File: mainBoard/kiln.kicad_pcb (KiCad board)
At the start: 4 copper layers, 203.1 x 114.5 mm, 214 parts, among them IC4 MAXM17572AMC+T, IC5 MAXM17572AMC+T, IC6 MAXM17572AMC+T, IC7 MAXM17572AMC+T, J1 1935161, J10 1935174, J11 1935174, J12 1935161, J13 SJ2-35813B-SMT-TR, J14 1935161, J15 SJ2-35813B-SMT-TR, J16 1935161, J17 SJ2-35813B-SMT-TR, J18 1935161, J19 1935161, J2 Conn_01x10_Pin, J20 1935161, J21 1935161, J23 1935161, J24 1935161, J25 1935161, J3 1935174, J4 1935174, J6 Conn_01x20_Socket, J7 Conn_02x06_Odd_Even, J8 1935174, K1 EE2-12NUH, K2 EE2-12NUH, K3 EE2-12NUH, K4 EE2-12NUH, K5 EE2-12NUH, Q1 BSS138P,215, Q2 BSS138P,215, Q3 BSS138P,215, Q4 BSS138P,215, Q5 BSS138P,215, U1 TCMT1109, U13 TCMT1109, U14 TCMT1109, U2 TCMT1109, U3 TCMT1109, U4 ESP32-S3-DevKitC, U5 SX1509, U7 AD8542, U8 AD8542, U9 AD8542

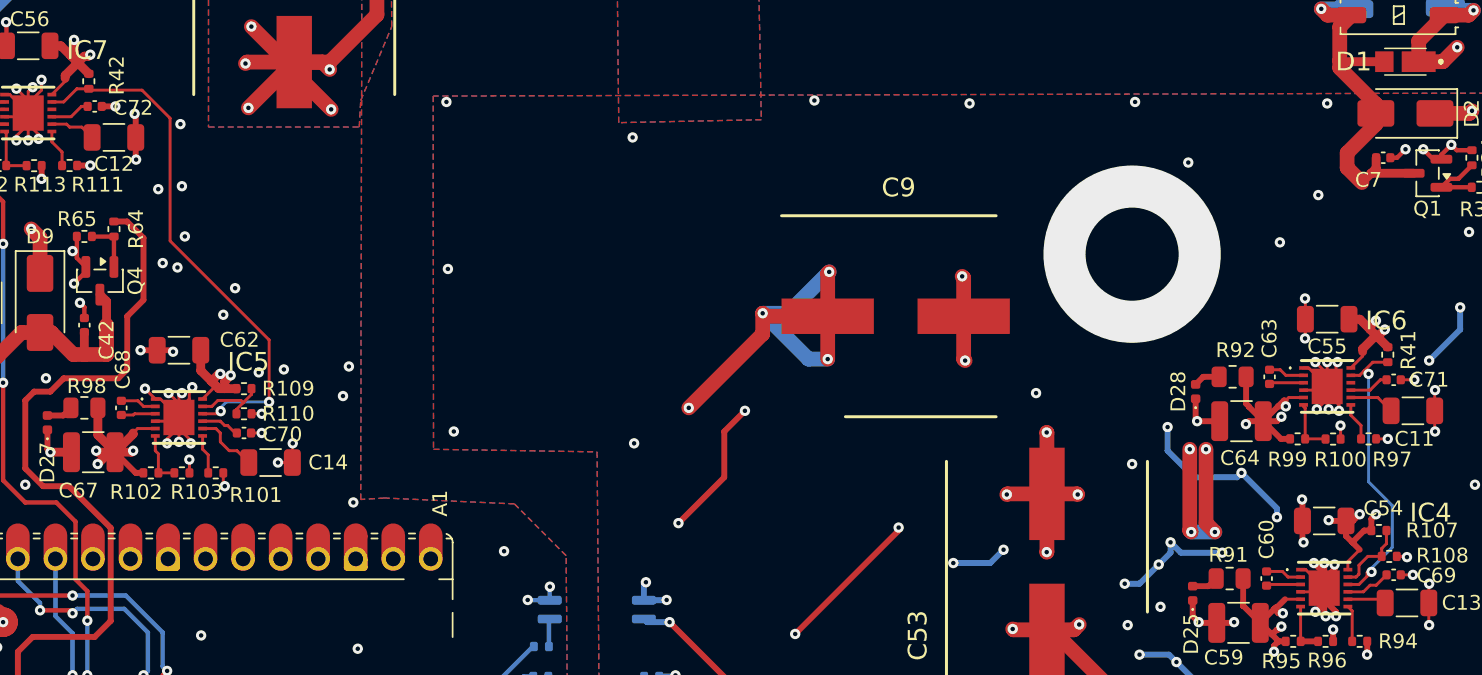
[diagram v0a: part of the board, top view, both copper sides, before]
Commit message: Update Board. removed power sequencing of 5v because it violated the voltage range of the power supply reset pin
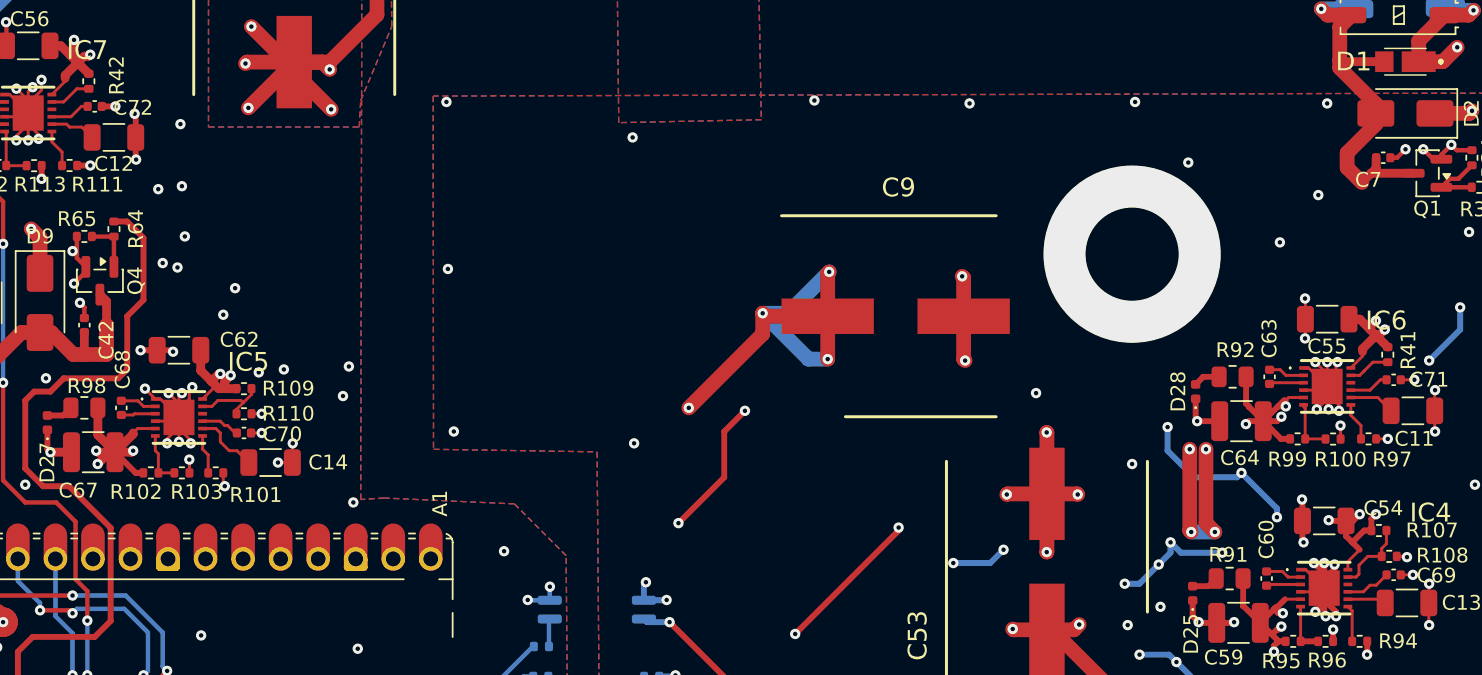
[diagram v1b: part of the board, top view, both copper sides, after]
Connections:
- IC4 pad 10: /5V Regulator/EN -> /MainRegulator/RESET
- IC5 pad 10: /Safty 5V Regulator/EN -> /SaftyRegulator/RESET
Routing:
- net /Safty 5V Regulator/EN: track 36.2 -> 3.00 mm, vias 2 -> 0
- net /5V Regulator/EN: track 20.0 -> 2.87 mm, vias 2 -> 0
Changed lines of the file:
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@@
 			(size 0.25 0.6)
 			(layers "F.Cu" "F.Mask" "F.Paste")
-			(net "/5V Regulator/EN")
+			(net "/MainRegulator/RESET")
 			(pinfunction "~{RESET}_10")
 			(pintype "passive")
@@
 			(size 0.25 0.6)
 			(layers "F.Cu" "F.Mask" "F.Paste")
-			(net "/Safty 5V Regulator/EN")
+			(net "/SaftyRegulator/RESET")
 			(pinfunction "~{RESET}_10")
 			(pintype "passive")
@@
 	)
 	(segment
-		(start 174.05 99.45)
-		(end 173.3 99.45)
-		(width 0.2)
-		(layer "F.Cu")
-		(net "/5V Regulator/EN")
-	)
-	(segment
 		(start 174.4 85)
 		(end 174.99 84.41)
@@
 	)
 	(segment
-		(start 174.6 98.65)
-		(end 174.6 98.9)
-		(width 0.2)
-		(layer "F.Cu")
-		(net "/5V Regulator/EN")
-	)
-	(segment
 		(start 174.99 84.41)
 		(end 176 84.41)
@@
 	)
 	(segment
-		(start 174.6 98.9)
-		(end 174.05 99.45)
-		(width 0.2)
-		(layer "F.Cu")
-		(net "/5V Regulator/EN")
-	)
-	(segment
-		(start 174.5 85)
-		(end 174.7 85.2)
-		(width 0.2)
-		(layer "F.Cu")
-		(net "/5V Regulator/EN")
-	)
-	(segment
 		(start 174.1 85.3)
 		(end 174.4 85)
@@
 	)
 	(segment
-		(start 174.65 98.6)
-		(end 174.6 98.65)
-		(width 0.2)
-		(layer "F.Cu")
-		(net "/5V Regulator/EN")
-	)
-	(segment
-		(start 174.4 85)
-		(end 174.5 85)
-		(width 0.2)
-		(layer "F.Cu")
-		(net "/5V Regulator/EN")
-	)
-	(segment
-		(start 174.9 98.6)
-		(end 174.65 98.6)
-		(width 0.2)
-		(layer "F.Cu")
-		(net "/5V Regulator/EN")
-	)
-	(segment
 		(start 173.5 85.3)
 		(end 174.1 85.3)
@@
 		(net "/5V Regulator/EN")
 	)
-	(via
-		(at 174.7 85.2)
-		(size 0.7)
-		(drill 0.3)
-		(layers "F.Cu" "B.Cu")
-		(net "/5V Regulator/EN")
-	)
-	(via
-		(at 174.9 98.6)
-		(size 0.7)
-		(drill 0.3)
-		(layers "F.Cu" "B.Cu")
-		(net "/5V Regulator/EN")
-	)
-	(segment
-		(start 174.7 92.5)
-		(end 174.7 85.2)
-		(width 0.2)
-		(layer "B.Cu")
-		(net "/5V Regulator/EN")
-	)
-	(segment
-		(start 174.9 98.6)
-		(end 174.9 98.35)
-		(width 0.2)
-		(layer "B.Cu")
-		(net "/5V Regulator/EN")
-	)
-	(segment
-		(start 174.9 98.35)
-		(end 176.3 96.95)
-		(width 0.2)
-		(layer "B.Cu")
-		(net "/5V Regulator/EN")
-	)
-	(segment
-		(start 176.3 94.1)
-		(end 174.7 92.5)
-		(width 0.2)
-		(layer "B.Cu")
-		(net "/5V Regulator/EN")
-	)
-	(segment
-		(start 176.3 96.95)
-		(end 176.3 94.1)
-		(width 0.2)
-		(layer "B.Cu")
-		(net "/5V Regulator/EN")
-	)
 	(segment
 		(start 173.6 96.6)
@@
 	)
 	(segment
-		(start 100.3 82.9)
-		(end 100.3 87.1)
-		(width 0.2)
-		(layer "F.Cu")
-		(net "/Safty 5V Regulator/EN")
-	)
-	(segment
-		(start 93.6 76.2)
-		(end 100.3 82.9)
-		(width 0.2)
-		(layer "F.Cu")
-		(net "/Safty 5V Regulator/EN")
-	)
-	(segment
 		(start 87.29 65.91)
 		(end 88.1 65.91)
@@
 	)
 	(segment
-		(start 95.8 87.9)
-		(end 96.84853 87.9)
-		(width 0.2)
-		(layer "F.Cu")
-		(net "/Safty 5V Regulator/EN")
-	)
-	(segment
 		(start 85.6 66.8)
 		(end 86.4 66.8)
@@
 	)
 	(segment
-		(start 91.7 66)
-		(end 93.6 67.9)
-		(width 0.2)
-		(layer "F.Cu")
-		(net "/Safty 5V Regulator/EN")
-	)
-	(segment
-		(start 96.84853 87.9)
-		(end 97.024265 87.724265)
-		(width 0.2)
-		(layer "F.Cu")
-		(net "/Safty 5V Regulator/EN")
-	)
-	(segment
-		(start 88.19 66)
-		(end 91.7 66)
-		(width 0.2)
-		(layer "F.Cu")
-		(net "/Safty 5V Regulator/EN")
-	)
-	(segment
 		(start 86.4 66.8)
 		(end 87.29 65.91)
@@
 	)
 	(segment
-		(start 93.6 67.9)
-		(end 93.6 76.2)
-		(width 0.2)
-		(layer "F.Cu")
-		(net "/Safty 5V Regulator/EN")
-	)
-	(via
-		(at 100.3 87.1)
-		(size 0.7)
-		(drill 0.3)
-		(layers "F.Cu" "B.Cu")
-		(net "/Safty 5V Regulator/EN")
-	)
-	(via
-		(at 97.024265 87.724265)
-		(size 0.7)
-		(drill 0.3)
-		(layers "F.Cu" "B.Cu")
-		(net "/Safty 5V Regulator/EN")
-	)
-	(segment
-		(start 97.4 87.1)
-		(end 96.9 87.6)
-		(width 0.2)
-		(layer "B.Cu")
-		(net "/Safty 5V Regulator/EN")
-	)
-	(segment
-		(start 96.9 87.6)
-		(end 97.024265 87.724265)
-		(width 0.2)
-		(layer "B.Cu")
-		(net "/Safty 5V Regulator/EN")
-	)
-	(segment
-		(start 100.3 87.1)
-		(end 97.4 87.1)
-		(width 0.2)
-		(layer "B.Cu")
-		(net "/Safty 5V Regulator/EN")
-	)
-	(segment
 		(start 192 71.75)
 		(end 192.25 72)
@@
 	)
 	(group ""
-		(members "0f56723d-3be1-4363-aa22-d1860701c7dc" "6eccc95b-070c-44a6-b1f1-dab8a373bad4"
-			"ecd03097-544e-4ff1-9250-bd5f418e28c1"
+		(members "0f56723d-3be1-4363-aa22-d1860701c7dc" "5a2fada0-188b-484a-bad7-1807c7aed6e5"
+			"6eccc95b-070c-44a6-b1f1-dab8a373bad4" "ecd03097-544e-4ff1-9250-bd5f418e28c1"
 		)
 	)
@@
 	)
 	(group ""
+		(members "396ff842-1671-4172-bf05-e17732549ce8" "4fc6aa10-2ebe-4c37-b5bb-b0deef5bf880"
+			"937600a3-2b20-4705-b469-8f8dcff22017" "b32b362c-9a1f-4c29-b6b9-67d3c509b282"
+		)
+	)
+	(group ""
 		(members "1354254c-1560-4867-a241-d6e0818e9545" "1dd019e7-ef0a-4e37-a044-a9138c332660"
 			"2d0f587a-aa5a-4280-accb-adcb2943fcc1" "61dba97c-334d-43c2-aecc-fc71d0e6a1a9"
@@
 		(members "1385005b-306d-4f59-b00a-3fc4f87c6aff" "472f01ce-623c-47e8-ad52-3c811087644f")
 	)
+	(group ""
+		(members "167178b8-de20-4731-a594-bc702b67bafe" "1fea3527-1d5b-4062-ab10-008cd30345a4"
+			"36329bb7-18b9-4f60-81fd-87c03581c975" "5ba218ab-53f7-4fd3-b41e-21470d26895f"
+			"74b8f7f9-8fd2-49d9-a18a-0e666f4fef0a" "8e096ba5-225d-4039-84e7-c9a3538eff79"
+		)
+	)
 	(embedded_fonts no)
